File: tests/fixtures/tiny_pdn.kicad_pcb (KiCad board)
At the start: 2 copper layers, 2 parts

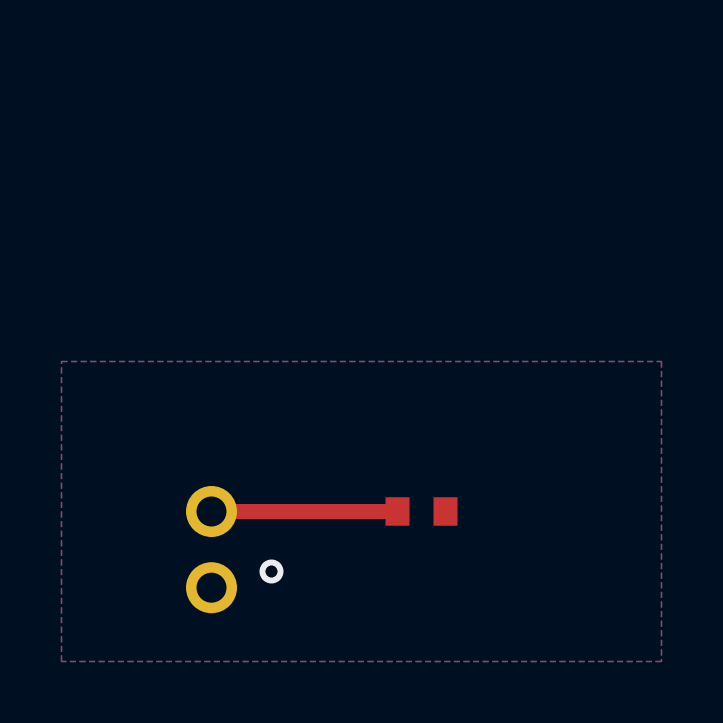
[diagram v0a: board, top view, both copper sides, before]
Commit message: Parse and render the board outline (Edge.Cuts layer)
Parser now collects gr_line / gr_arc / gr_circle on Edge.Cuts into
model::Board::outline as straight-line segments. Arcs and circles are
sampled into polylines at parse time (24 segs per arc, 48 per circle)
so the renderer only needs to draw lines.

Arc geometry derived from KiCads (start, mid, end) form via a 3-point
circle fit (perpendicular bisector intersection), then swept the
direction that passes through the mid point. Collinear inputs fall
back to a single straight segment.

PcbCanvas gained outline_vbo_ + outline_vao_ populated in buildOutline
on setBoard. Rendered as light-gray (0.85,0.85,0.88) lines after the
grid and before the per-layer copper fills — gives the user a visible
board boundary at every zoom level instead of having to infer it from
where copper happens to exist.

Fixture extended with a 20x10mm rectangle + one arc + one circle on
Edge.Cuts; e2e test verifies the parsed segment count (76) and that
the first segment matches the expected bottom edge. Total: 93/93.
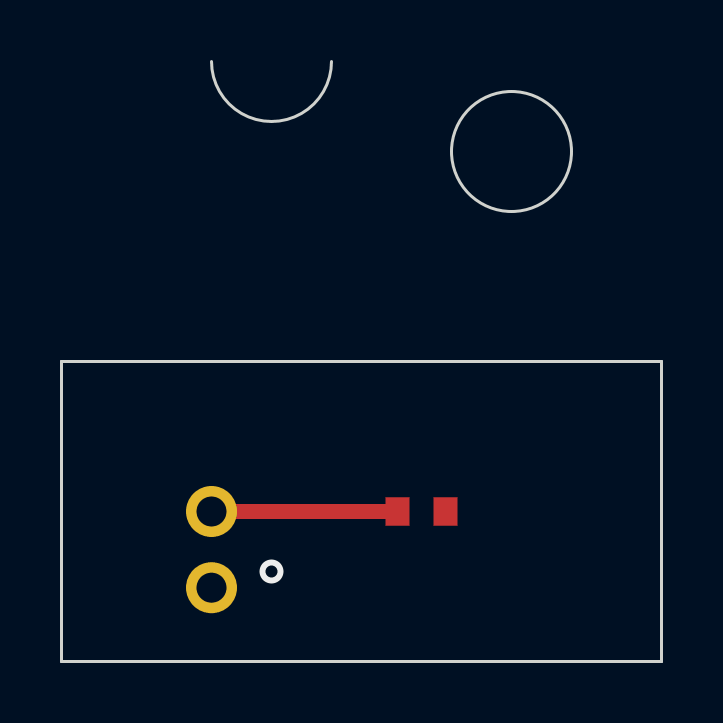
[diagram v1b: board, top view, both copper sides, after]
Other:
- board outline added: 20 x 20 mm
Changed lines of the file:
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@@
         )
     )
+    (gr_line (start 0 15) (end 20 15) (layer "Edge.Cuts") (width 0.1))
+    (gr_line (start 20 15) (end 20 25) (layer "Edge.Cuts") (width 0.1))
+    (gr_line (start 20 25) (end 0 25) (layer "Edge.Cuts") (width 0.1))
+    (gr_line (start 0 25) (end 0 15) (layer "Edge.Cuts") (width 0.1))
+    (gr_arc (start 5 5) (mid 7 7) (end 9 5) (layer "Edge.Cuts") (width 0.1))
+    (gr_circle (center 15 8) (end 17 8) (layer "Edge.Cuts") (width 0.1))
 )
